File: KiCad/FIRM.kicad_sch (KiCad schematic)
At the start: 65 parts, among them J1 Conn_01x04_Pin, J3 Micro_SD_Card_Det2, J5 USB_C_Receptacle_USB2.0_16P, Q1 AO3401A, U1 STM32F405RGTx, U6 AP2112K-3.3, U7 W25Q128JVS, X2 32.768khz, Y1 12mhz

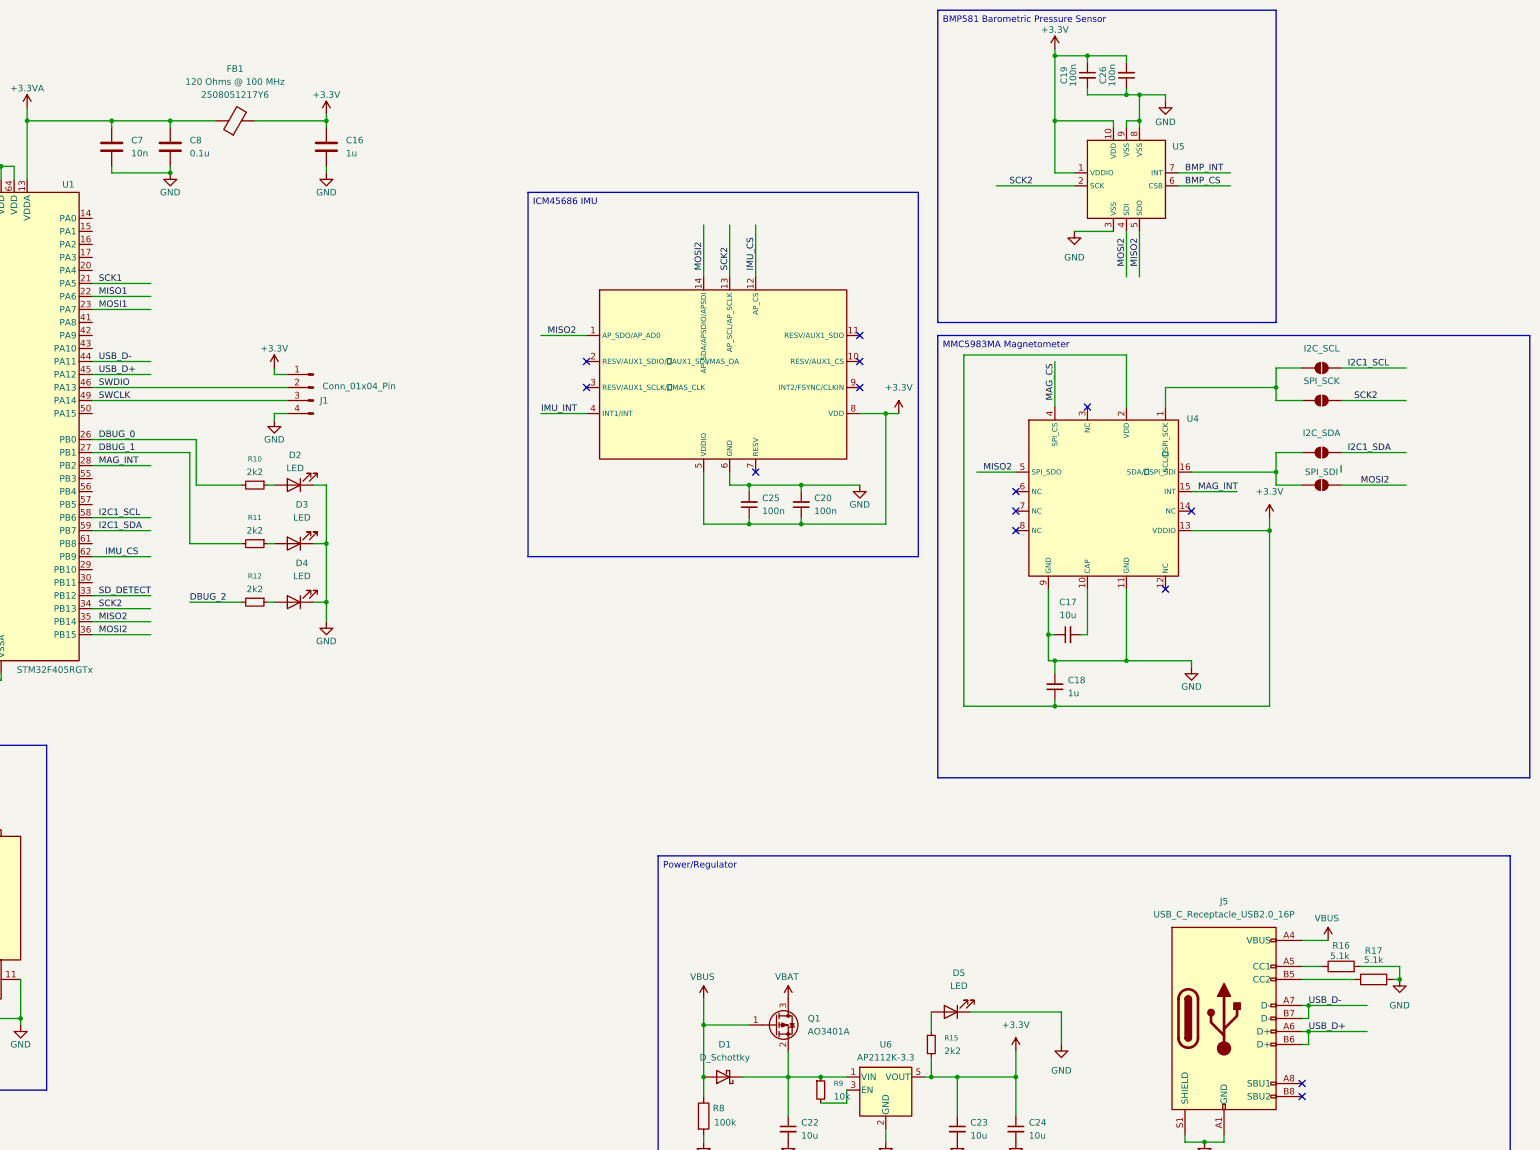
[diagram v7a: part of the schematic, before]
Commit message: LEDs, reset button, i2c pullups
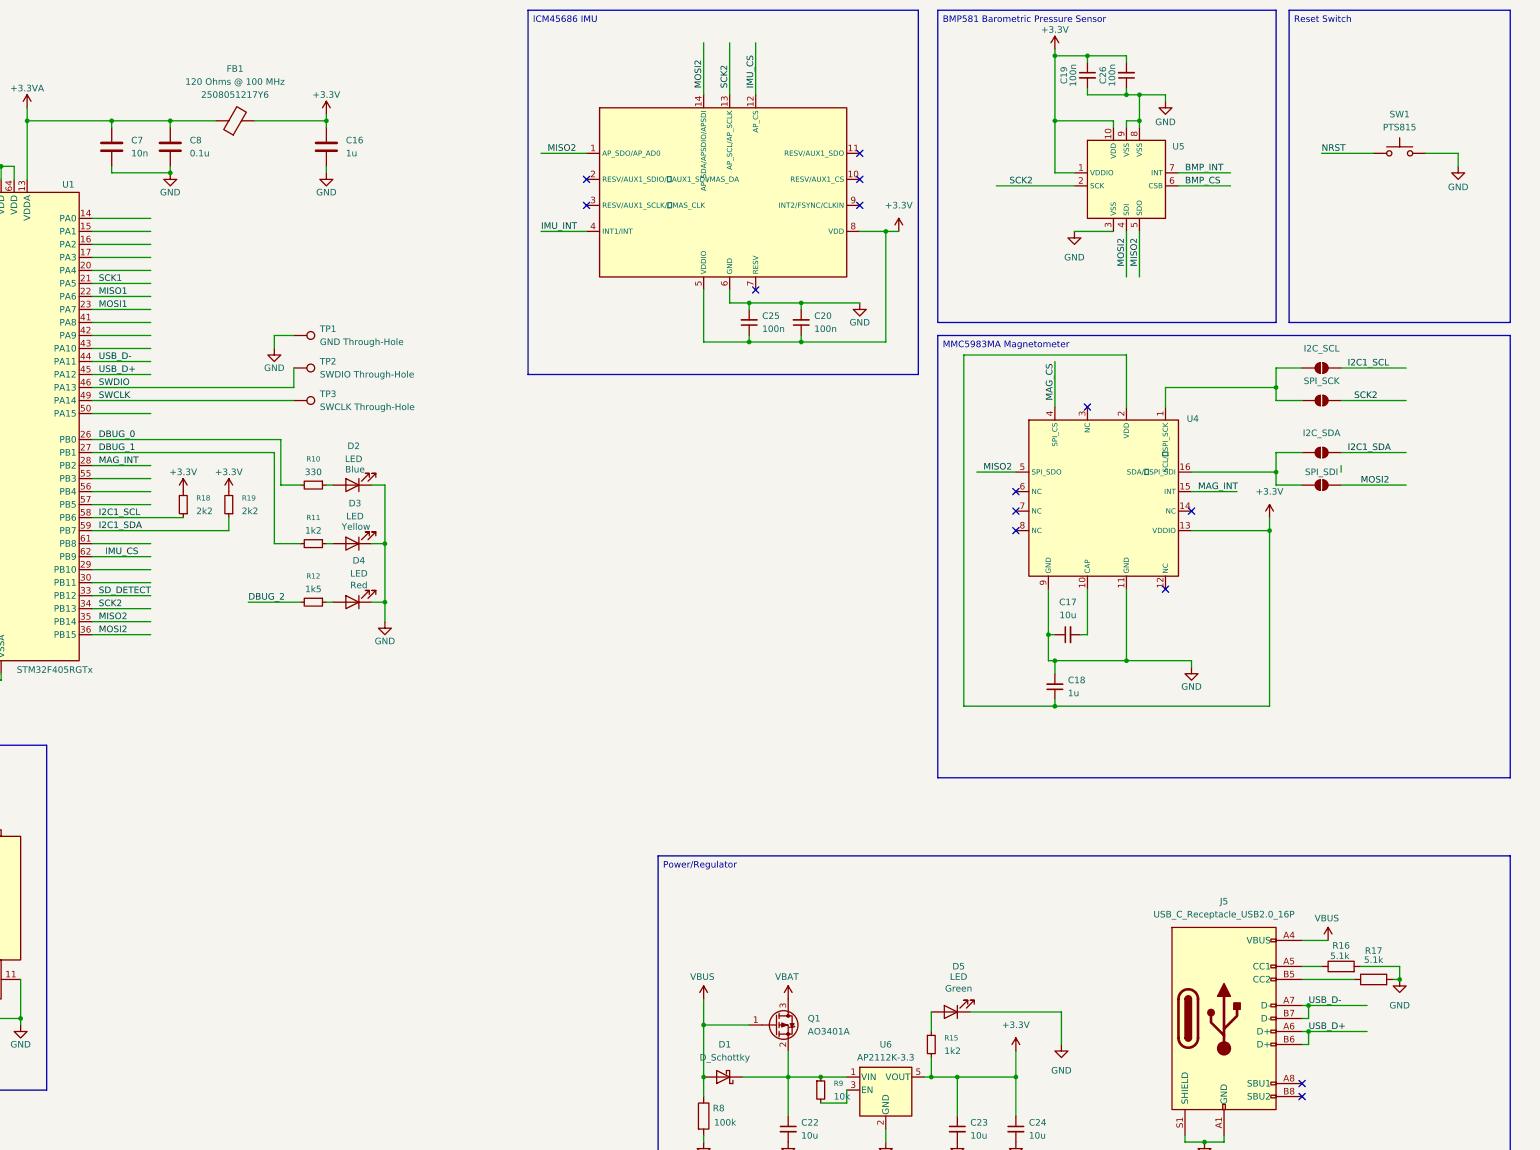
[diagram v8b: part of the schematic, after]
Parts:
- removed J1: Conn_01x04_Pin, symbol Connector:Conn_01x04_Pin
- added R18, R19: 2k2, symbol Device:R_Small
- added SW1: PTS815, symbol Switch:SW_Push
- added TP1: GND Through-Hole, symbol Connector:TestPoint
- added TP2: SWDIO Through-Hole, symbol Connector:TestPoint
- added TP3: SWCLK Through-Hole, symbol Connector:TestPoint
- R10: value 2k2 -> 330
- R11, R15: value 2k2 -> 1k2
- R12: value 2k2 -> 1k5
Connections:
- net +3.3V: now also R18.2, R19.2
- net GND: now also SW1.2, TP1.1
- net I2C1_SCL: now also R18.1
- net I2C1_SDA: now also R19.1
- net NRST: now also SW1.1
- net SWCLK: now also TP3.1
- net SWDIO: now also TP2.1
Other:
- moved on the sheet: C20, C25, D2, D3, D4, R10, R11, R12
